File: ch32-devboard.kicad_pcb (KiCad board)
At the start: 2 copper layers, 29.2 x 39 mm, 19 parts, among them J1 Conn_01x10_Pin, J2 Conn_01x05_Pin, J3 Conn_01x10_Pin, J4 USB_C_Receptacle_USB2.0_16P, J5 Conn_01x03_Socket, SW1 CK_KMS2xxG, U1 AP2112K-3.3

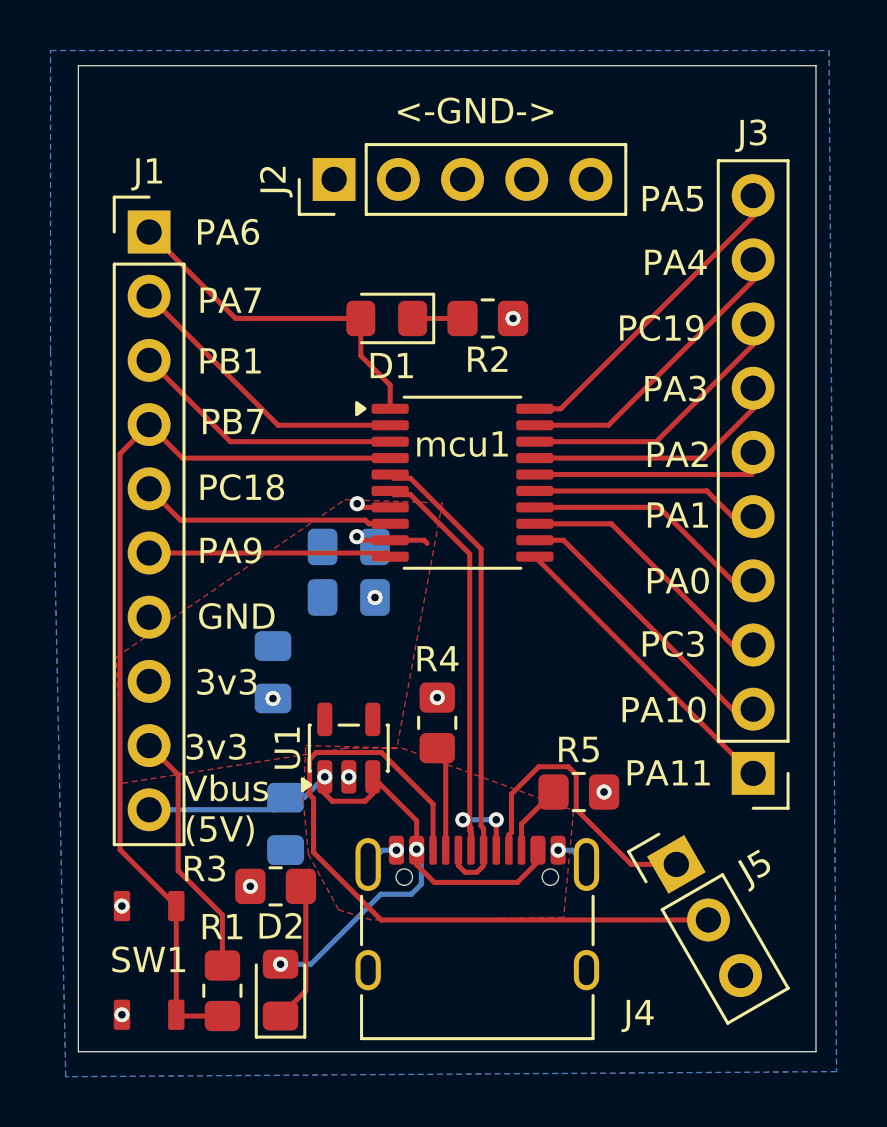
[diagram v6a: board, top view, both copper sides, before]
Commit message: boot button, add drill data to exports, change usb C footprint
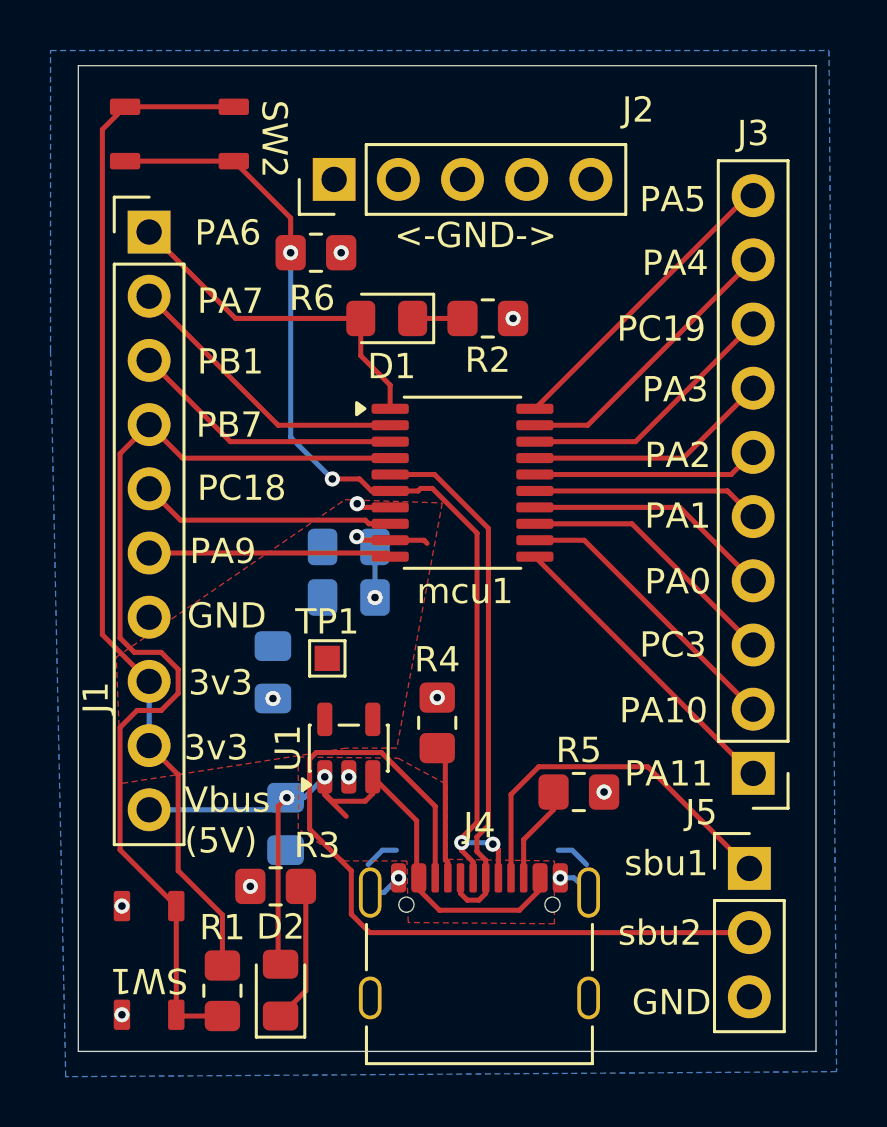
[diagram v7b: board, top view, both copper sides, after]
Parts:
- added R6: 10k, Resistor_SMD:R_0805_2012Metric_Pad1.20x1.40mm_HandSolder, F.Cu at (142.2, 72.9)
- added SW2: SW_Push, ch32-devBoard-symbols:smd-push-button-TS3425PA, F.Cu at (136.8, 68.2)
- added TP1: VDD(3v3), TestPoint:TestPoint_Pad_1.0x1.0mm, F.Cu at (142.7, 89.0)
- J4: footprint Connector_USB:USB_C_Receptacle_XKB_U262-16XN-4BVC11 -> Connector_USB:USB_C_Receptacle_Palconn_UTC16-G
- SW1: value CK_KMS2xxG -> SW_Push; footprint CH32-devBoard:smd-push-button-TS3425PA -> ch32-devBoard-symbols:smd-push-button-TS3425PA
- moved J5 2.89 mm to (159.3, 97.3), turned to 0 degrees
- moved J4 0.11 mm to (148.7, 100.1)
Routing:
- net /VDD: track 14.2 -> 46.3 mm
- net /UD+: track 19.8 -> 41.9 mm, vias 2 -> 4
- net Net-(J4-SBU2): track 28.1 -> 31.7 mm
- net Net-(J4-SBU1): track 11.6 -> 14.9 mm
- net /PB7: track 36.7 -> 39.7 mm
- net GND: track 4.07 -> 6.79 mm, vias 10 -> 11
- net /UD-: track 19.2 -> 21.4 mm
- net Net-(J4-CC1): track 3.70 -> 4.86 mm
- net Net-(J4-CC2): track 2.83 -> 3.89 mm
- net /PA5: track 12.6 -> 11.9 mm
- net /Vbus: track 28.2 -> 28.5 mm, vias 3 -> 2
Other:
- board text added: "sbu1"
- board text added: "sbu2"
